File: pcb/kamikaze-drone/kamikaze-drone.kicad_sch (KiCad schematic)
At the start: 4 parts, among them U1 STM32F765VITx, U2 LSM6DSL, U3 BMP280, U4 M95512-Axxx-MF

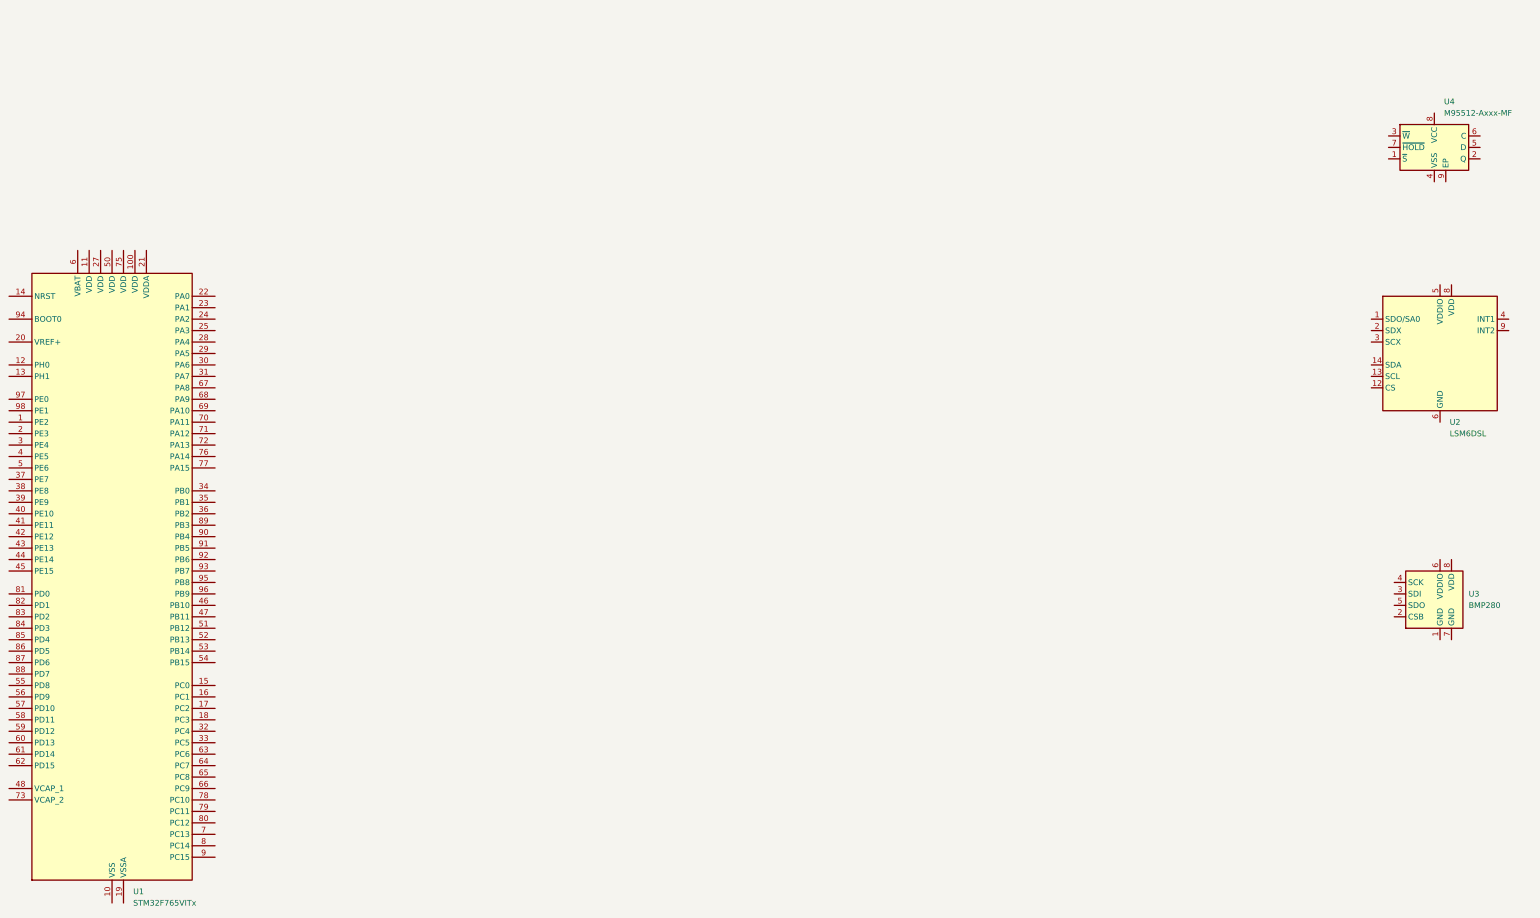
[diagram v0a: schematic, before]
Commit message: v1 of PCB completed
Complete schematic completed with motor drivers, sensor integration and
others.
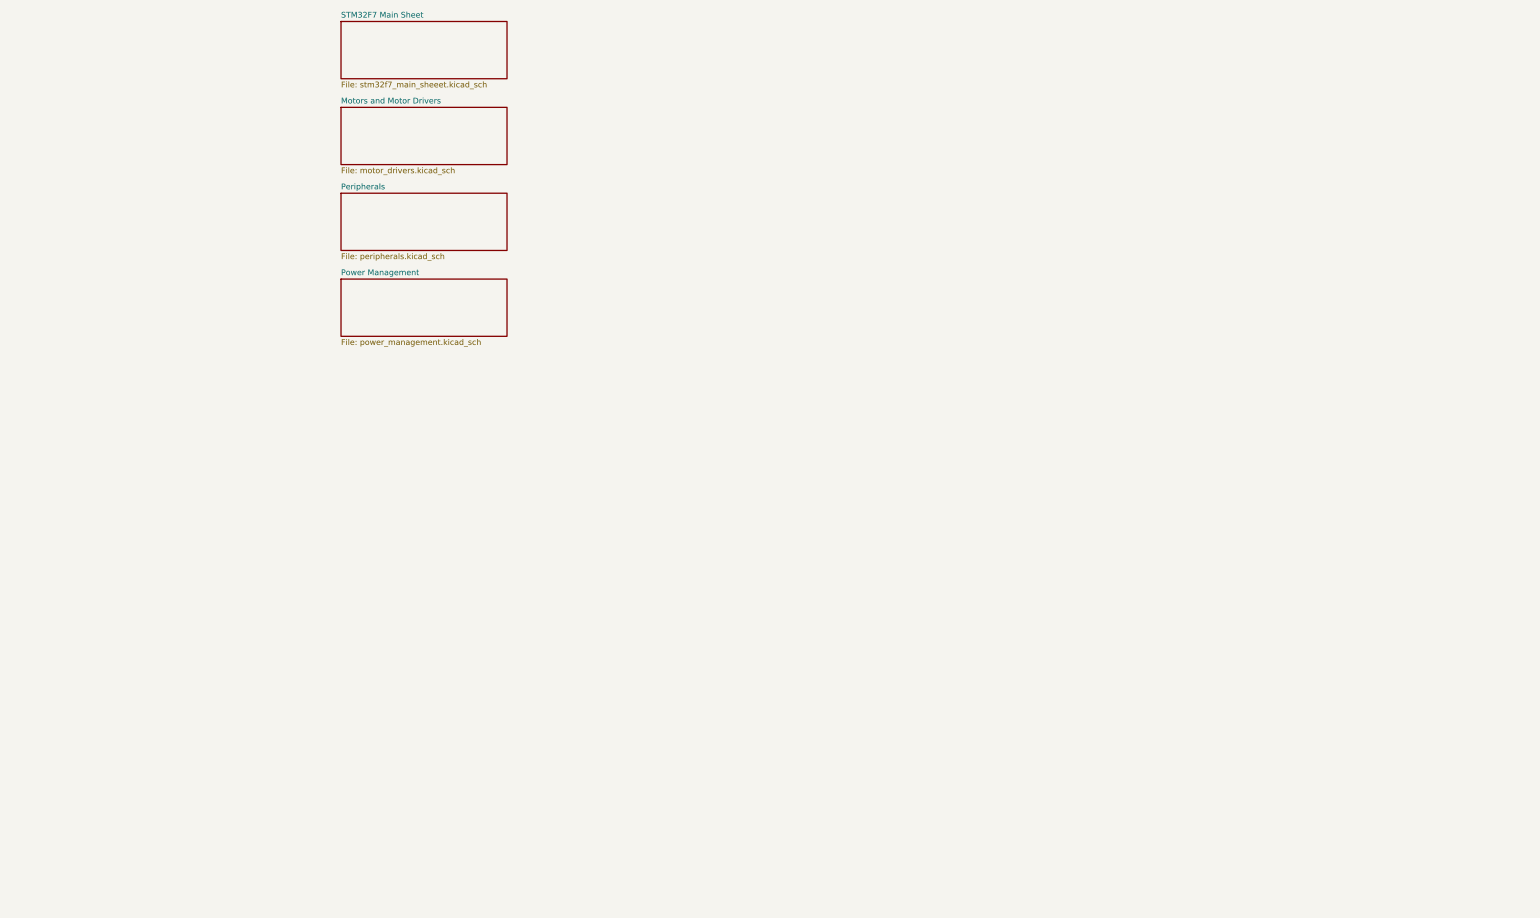
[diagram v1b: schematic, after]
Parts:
- removed U1: STM32F765VITx, Package_QFP:LQFP-100_14x14mm_P0.5mm, symbol MCU_ST_STM32F7:STM32F765VITx
- removed U2: LSM6DSL, Package_LGA:LGA-14_3x2.5mm_P0.5mm_LayoutBorder3x4y, symbol Sensor_Motion:LSM6DSL
- removed U3: BMP280, Package_LGA:Bosch_LGA-8_2x2.5mm_P0.65mm_ClockwisePinNumbering, symbol Sensor_Pressure:BMP280
- removed U4: M95512-Axxx-MF, Package_DFN_QFN:WFDFPN-8-1EP_3x2mm_P0.5mm_EP1.25x1.35mm, symbol Memory_EEPROM:M95512-Axxx-MF
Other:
- added sheet Motors and Motor Drivers (motor_drivers.kicad_sch)
- added sheet Peripherals (peripherals.kicad_sch)
- added sheet Power Management (power_management.kicad_sch)
- added sheet STM32F7 Main Sheet (stm32f7_main_sheeet.kicad_sch)
- company: (none) -> Pranav Chandra N. V.
- title: (none) -> Kamikaze Drone
